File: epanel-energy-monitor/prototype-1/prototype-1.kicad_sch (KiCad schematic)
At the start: 39 parts, among them J1 Conn_01x05_Male, J2 Screw_Terminal_01x03, J3 Screw_Terminal_01x03, Q1 IRF830, Q2 IRF830, Q3 IRF830, Q4 IRF830, U1 Pico, U2 4N35, U3 4N35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

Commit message: wip
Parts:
- removed C2: 2.2uF/63V, Capacitor_SMD:C_1206_3216Metric, symbol Device:C_Polarized
- removed D2: 10V/0.4W, Diode_SMD:D_SOD-123, symbol Diode:BZV55B10
- removed D4: 1N4007, Diode_SMD:D_SMA, symbol Diode:1N4007
- removed J2, J3: Screw_Terminal_01x03, TerminalBlock:TerminalBlock_bornier-3_P5.08mm, symbol Connector:Screw_Terminal_01x03
- removed Q3, Q4: IRF830, Package_TO_SOT_SMD:TO-263-3_TabPin2, symbol Transistor_FET:IRF740
- removed R12, R13, R14, R15, R17, R9: 33KΩ/0.5W, Resistor_SMD:R_0805_2012Metric, symbol Device:R
- removed R2: 330Ω, Resistor_SMD:R_0603_1608Metric, symbol Device:R
- removed R4, R5: 10KΩ, Resistor_SMD:R_0603_1608Metric, symbol Device:R
- removed R7: 22KΩ, Resistor_SMD:R_0603_1608Metric, symbol Device:R
- removed U3: 4N35, Package_DIP:SMDIP-6_W7.62mm, symbol Isolator:4N35
- removed U5, U6: H11AA1, Package_DIP:SMDIP-6_W9.53mm, symbol Isolator:H11AA1
- added R? (x2): 10KΩ, Resistor_SMD:R_0603_1608Metric, symbol Device:R
- added R?: 4.7KΩ, Resistor_SMD:R_0603_1608Metric, symbol Device:R
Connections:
- net LINE: now also J?.1 (Pin_1)
- net NEUT: now also J?.2 (Pin_2)
- net at R3.1, U4.5: no longer U1.19 (GPIO14)
- net at U1.20 (GPIO15): no longer R1.2
- no-connect marks 5 -> 2
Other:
- note removed: "Button sensor 1"
- note removed: "Dimmer 1"
- note removed: "Zero crossing detector"
- moved on the sheet: C1, D1, D3, Q1, Q2, R1, R10, R11, R16, R3, R6, R8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

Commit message: add teleinfo schematic
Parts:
- added J?: Screw_Terminal_01x02, symbol Connector:Screw_Terminal_01x02
- added Q?: BS170, Package_TO_SOT_THT:TO-92_Inline, symbol Transistor_FET:BS170
- added U?: LTV-814, Package_DIP:DIP-4_W7.62mm, symbol Isolator:LTV-814
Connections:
- net +3V3: now also R?.2, U?.4
- net GND: now also R?.1, Q?.3 (S)
- net at R?.2: now also Q?.2 (G), U?.3
- net at R?.1: now also J?.1 (Pin_1)
- net at R?.2: now also U?.1
- net at R?.1: now also Q?.1 (D)
- new net: J?.2 (Pin_2), U?.2
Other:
- note added: "Teleinfo"
- moved on the sheet: J?, R?

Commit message: wip energy monitor
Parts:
- removed C1: 2.2uF/63V, Capacitor_SMD:C_1206_3216Metric, symbol Device:C_Polarized
- removed D1: 10V/0.4W, Diode_SMD:D_SOD-123, symbol Diode:BZV55B10
- removed D3: 1N4007, Diode_SMD:D_SMA, symbol Diode:1N4007
- removed Q1, Q2: IRF830, Package_TO_SOT_SMD:TO-263-3_TabPin2, symbol Transistor_FET:IRF740
- removed R1: 330Ω, Resistor_SMD:R_0603_1608Metric, symbol Device:R
- removed R10, R11, R16, R8: 33KΩ/0.5W, Resistor_SMD:R_0805_2012Metric, symbol Device:R
- removed R3: 10KΩ, Resistor_SMD:R_0603_1608Metric, symbol Device:R
- removed R6: 22KΩ, Resistor_SMD:R_0603_1608Metric, symbol Device:R
- removed U2: 4N35, Package_DIP:SMDIP-6_W7.62mm, symbol Isolator:4N35
- removed U4: H11AA1, Package_DIP:SMDIP-6_W9.53mm, symbol Isolator:H11AA1
- added C? (x2): 10uF/6V, symbol Device:C
- added J? (x2): AudioJack2_Ground, symbol Connector:AudioJack2_Ground
- added R? (x4): 470KΩ, Resistor_SMD:R_0603_1608Metric, symbol Device:R
- added R?: 22Ω, symbol Device:R
- added R? (x2): 1KΩ, Resistor_SMD:R_0603_1608Metric, symbol Device:R
- added R?: 120Ω, symbol Device:R
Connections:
- net +3V3: now also R?.2, R?.2
- net GND: now also C?.2, C?.2, R?.1, R?.1
- new net: J?.G, R?.1, R?.2 (x2)
- new net: C?.1, J?.T, R?.1, R?.2, R?.2 (x2)
- no-connect marks 2 -> 0
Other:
- note added: "CT 23kW max - YHDC SCT-013-00"
- note added: "CT 4kW max - YHDC SCT-013-00"
- note removed: "Button sensor 0"
- note removed: "Dimmer 0"

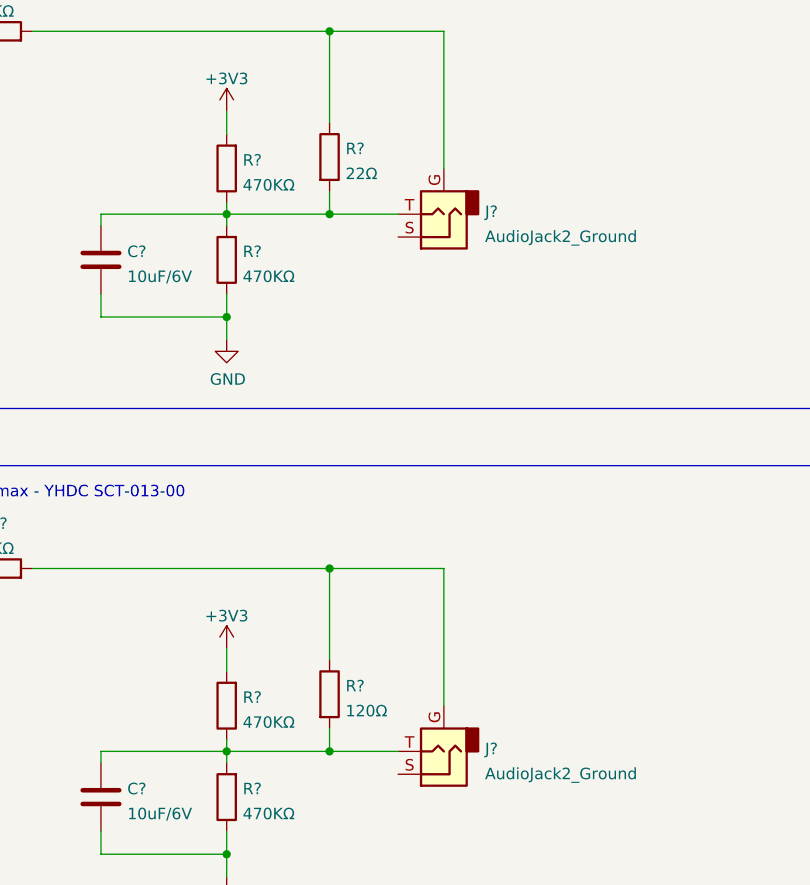
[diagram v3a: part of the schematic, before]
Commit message: add R power
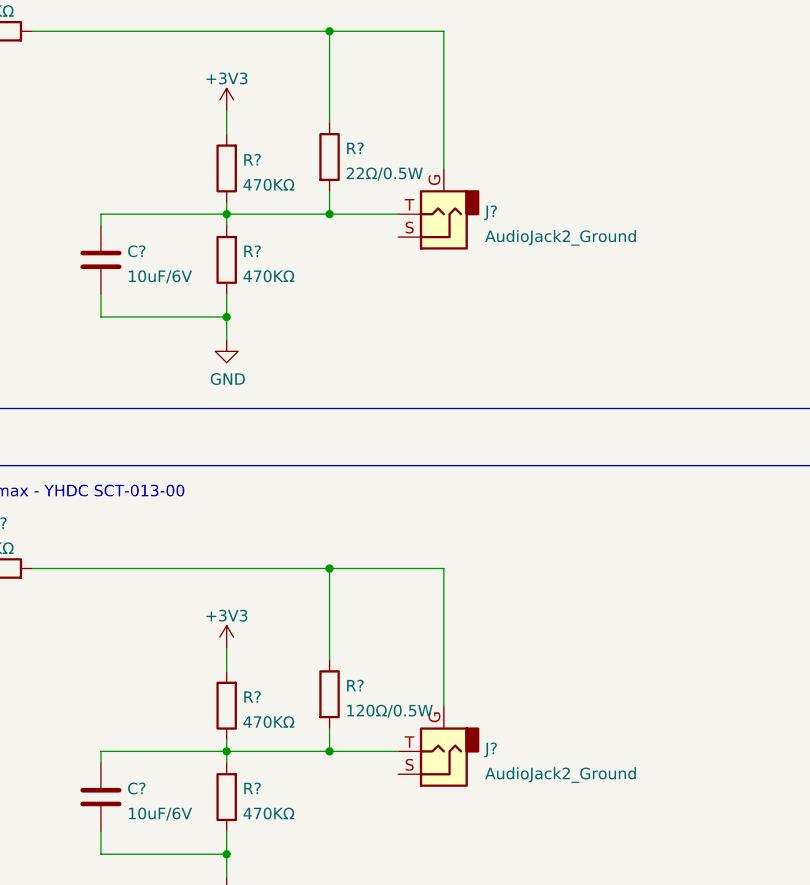
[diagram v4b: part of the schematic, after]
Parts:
- R?: value 22Ω -> 22Ω/0.5W
- R?: value 120Ω -> 120Ω/0.5W
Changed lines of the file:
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@@
       (effects (font (size 1.27 1.27)) (justify left))
     )
-    (property "Value" "22Ω" (id 1) (at 339.598 133.9466 0)
+    (property "Value" "22Ω/0.5W" (id 1) (at 339.598 133.9466 0)
       (effects (font (size 1.27 1.27)) (justify left))
     )
@@
       (effects (font (size 1.27 1.27)) (justify left))
     )
-    (property "Value" "120Ω" (id 1) (at 339.598 193.6366 0)
+    (property "Value" "120Ω/0.5W" (id 1) (at 339.598 193.6366 0)
       (effects (font (size 1.27 1.27)) (justify left))
     )
@@
     )
     (path "/61d13227-ea38-4175-a5c0-8f75a3d5765d"
-      (reference "R?") (unit 1) (value "22Ω") (footprint "")
+      (reference "R?") (unit 1) (value "22Ω/0.5W") (footprint "")
     )
     (path "/79669be6-ff4f-4a0d-ab0f-2e84ce7f2aa3"
@@
     )
     (path "/c617335c-bbb9-4ba2-bf32-96285610c756"
-      (reference "R?") (unit 1) (value "120Ω") (footprint "")
+      (reference "R?") (unit 1) (value "120Ω/0.5W") (footprint "")
     )
     (path "/eb97f50e-7ea5-4f23-a809-258cd91d8cb4"

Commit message: wip footprints
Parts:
- removed J1: Conn_01x05_Male, Connector_PinHeader_2.54mm:PinHeader_1x05_P2.54mm_Vertical, symbol Connector:Conn_01x05_Male
- removed JP1: Jumper_2_Bridged, Connector_PinHeader_2.54mm:PinHeader_1x02_P2.54mm_Vertical, symbol Jumper:Jumper_2_Bridged
- removed U1: Pico, MCU_RaspberryPi_and_Boards:RPi_Pico_SMD_TH, symbol MCU_RaspberryPi_and_Boards:Pico
- added J1: Conn_01x06_Male, Connector_PinHeader_2.54mm:PinHeader_1x06_P2.54mm_Vertical, symbol Connector:Conn_01x06_Male
- C1, C2: renamed from C?; footprint (none) -> Resistor_SMD:R_0603_1608Metric; LCSC (none) -> C96446
- J4, J5: renamed from J?; footprint (none) -> TerminalBlock:TerminalBlock_bornier-2_P5.08mm
- Q1: renamed from Q?; footprint Package_TO_SOT_THT:TO-92_Inline -> Package_TO_SOT_SMD:SOT-23; LCSC (none) -> C151050
- R1, R2: renamed from R?; LCSC (none) -> C21190
- R10: renamed from R?; footprint (none) -> Resistor_SMD:R_0805_2012Metric; LCSC (none) -> C966144
- R11: renamed from R?; LCSC (none) -> C23162
- R4, R5, R6, R7: renamed from R?; LCSC (none) -> C23178
- R9: renamed from R?; footprint (none) -> Resistor_SMD:R_0805_2012Metric; LCSC (none) -> C441970
- U1: renamed from U?; footprint Package_DIP:DIP-4_W7.62mm -> Package_DIP:SMDIP-4_W7.62mm; LCSC (none) -> C2829070
- gave numbers to parts that had none: 4
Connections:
- net +3V3: now also J1.2 (Pin_2)
- net +5V: now also J1.1 (Pin_1)
- net GND: now also J1.3 (Pin_3)
- net at Q1.1 (D), R3.1: now also J1.4 (Pin_4)
- net at R2.1: now also J1.6 (Pin_6)
- net at R1.1: now also J1.5 (Pin_5)
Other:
- note added: "CT0 23kW max - YHDC SCT-013-00"
- note added: "CT1 4kW max - YHDC SCT-013-00"
- note removed: "CT 23kW max - YHDC SCT-013-00"
- note removed: "CT 4kW max - YHDC SCT-013-00"
- moved on the sheet: C1, C2, J2, J3, J4, J5, PS1, Q1, R1, R10, R11, R2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

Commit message: first test
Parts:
- J2, J3: footprint (none) -> Connector_Audio:Jack_3.5mm_PJ320D_Horizontal; LCSC (none) -> C521460
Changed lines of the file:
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@@
       (effects (font (size 1.27 1.27)) (justify right))
     )
-    (property "Footprint" "" (id 2) (at 247.65 204.47 0)
-      (effects (font (size 1.27 1.27)) hide)
-    )
-    (property "Datasheet" "~" (id 3) (at 247.65 204.47 0)
+    (property "Footprint" "Connector_Audio:Jack_3.5mm_PJ320D_Horizontal" (id 2) (at 247.65 204.47 0)
+      (effects (font (size 1.27 1.27)) hide)
+    )
+    (property "Datasheet" "https://datasheet.lcsc.com/lcsc/2005041005_USAKRO-PJ-320D_C521460.pdf" (id 3) (at 247.65 204.47 0)
+      (effects (font (size 1.27 1.27)) hide)
+    )
+    (property "LCSC" "C521460" (id 4) (at 247.65 204.47 0)
       (effects (font (size 1.27 1.27)) hide)
     )
@@
       (effects (font (size 1.27 1.27)) (justify right))
     )
-    (property "Footprint" "" (id 2) (at 247.65 144.78 0)
-      (effects (font (size 1.27 1.27)) hide)
-    )
-    (property "Datasheet" "~" (id 3) (at 247.65 144.78 0)
+    (property "Footprint" "Connector_Audio:Jack_3.5mm_PJ320D_Horizontal" (id 2) (at 247.65 144.78 0)
+      (effects (font (size 1.27 1.27)) hide)
+    )
+    (property "Datasheet" "https://datasheet.lcsc.com/lcsc/2005041005_USAKRO-PJ-320D_C521460.pdf" (id 3) (at 247.65 144.78 0)
+      (effects (font (size 1.27 1.27)) hide)
+    )
+    (property "LCSC" "C521460" (id 4) (at 247.65 144.78 0)
       (effects (font (size 1.27 1.27)) hide)
     )
@@
     )
     (path "/987b82f6-d839-4bd5-9b0d-6bfcf7572b6c"
-      (reference "J2") (unit 1) (value "AudioJack2_Ground") (footprint "")
+      (reference "J2") (unit 1) (value "AudioJack2_Ground") (footprint "Connector_Audio:Jack_3.5mm_PJ320D_Horizontal")
     )
     (path "/256c13ca-f13e-4983-8c7f-dcdd0fd59a7c"
-      (reference "J3") (unit 1) (value "AudioJack2_Ground") (footprint "")
+      (reference "J3") (unit 1) (value "AudioJack2_Ground") (footprint "Connector_Audio:Jack_3.5mm_PJ320D_Horizontal")
     )
     (path "/b17590ac-bb78-4798-b20d-40942eeb2176"

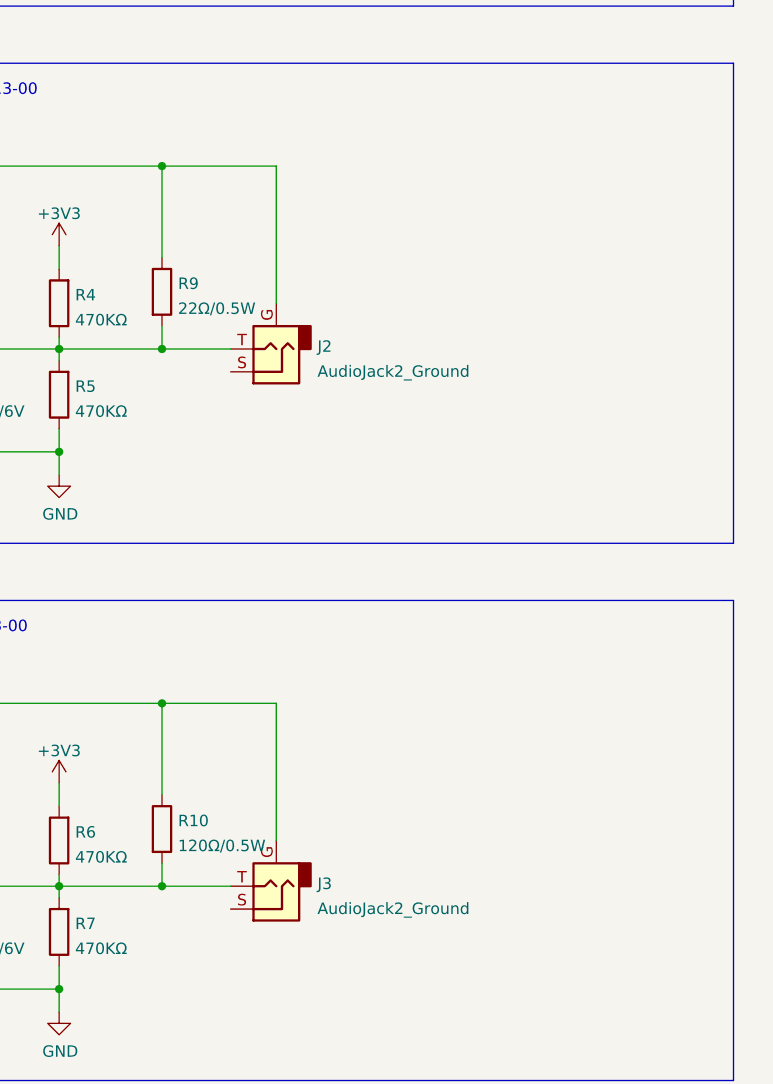
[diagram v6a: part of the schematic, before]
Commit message: add headers in case jack pinout is wrong
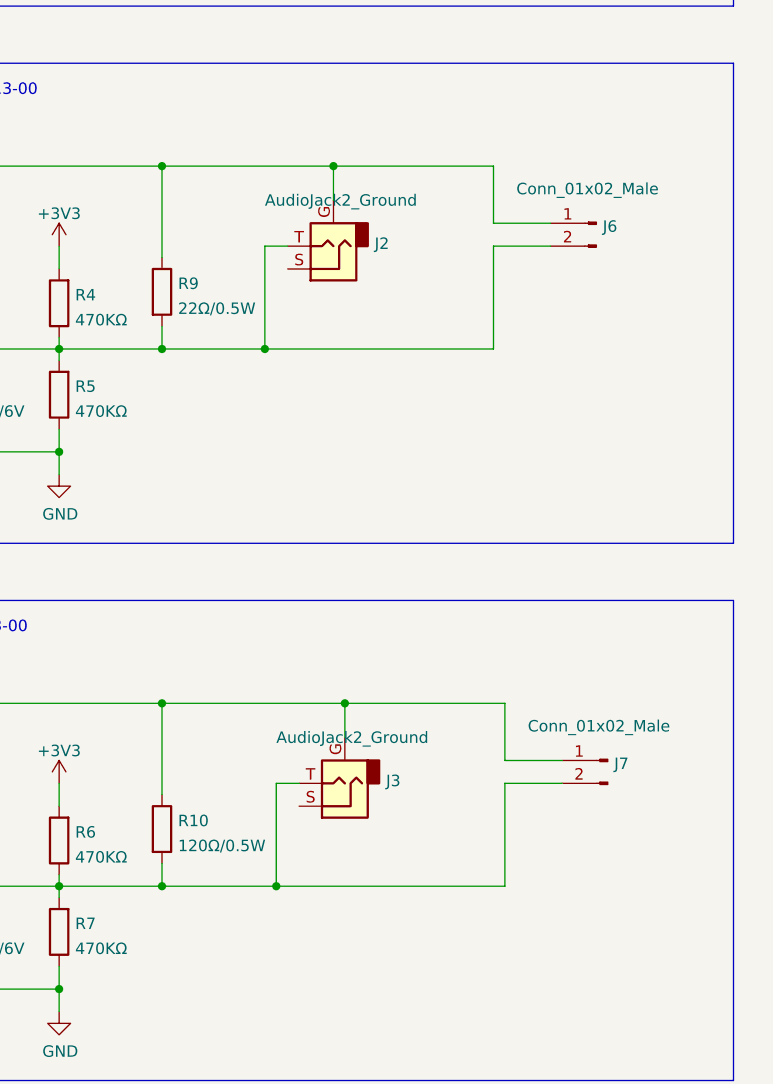
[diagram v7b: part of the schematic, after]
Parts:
- added J6, J7: Conn_01x02_Male, symbol Connector:Conn_01x02_Male
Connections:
- net at J3.G, R10.1, R2.2: now also J7.1 (Pin_1)
- net at C2.1, J3.T, R10.2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: now also J7.2 (Pin_2)
- net at J2.G, R1.2, R9.1: now also J6.1 (Pin_1)
- net at C1.1, J2.T, R4.1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: now also J6.2 (Pin_2)
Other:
- moved on the sheet: J2

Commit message: wip
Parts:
- J6, J7: footprint (none) -> Connector_PinHeader_2.54mm:PinHeader_1x02_P2.54mm_Vertical
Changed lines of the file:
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@@
       (effects (font (size 1.27 1.27)) (justify right))
     )
-    (property "Footprint" "" (id 2) (at 283.21 130.81 0)
+    (property "Footprint" "Connector_PinHeader_2.54mm:PinHeader_1x02_P2.54mm_Vertical" (id 2) (at 283.21 130.81 0)
       (effects (font (size 1.27 1.27)) hide)
     )
@@
       (effects (font (size 1.27 1.27)) (justify right))
     )
-    (property "Footprint" "" (id 2) (at 284.48 190.5 0)
+    (property "Footprint" "Connector_PinHeader_2.54mm:PinHeader_1x02_P2.54mm_Vertical" (id 2) (at 284.48 190.5 0)
       (effects (font (size 1.27 1.27)) hide)
     )
@@
     )
     (path "/75fb2c3a-e486-423a-935f-1fb07328359e"
-      (reference "J6") (unit 1) (value "Conn_01x02_Male") (footprint "")
+      (reference "J6") (unit 1) (value "Conn_01x02_Male") (footprint "Connector_PinHeader_2.54mm:PinHeader_1x02_P2.54mm_Vertical")
     )
     (path "/f0fcb2f0-4bec-4a32-83dd-ac07bfcfbf9c"
-      (reference "J7") (unit 1) (value "Conn_01x02_Male") (footprint "")
+      (reference "J7") (unit 1) (value "Conn_01x02_Male") (footprint "Connector_PinHeader_2.54mm:PinHeader_1x02_P2.54mm_Vertical")
     )
     (path "/eab3c1d2-8494-4933-98a0-1f180f0c6f69"
